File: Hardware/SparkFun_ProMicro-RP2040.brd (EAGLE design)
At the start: 17.8 x 33 mm, 109 parts, among them J2 Qwiic, J5 USB Female Type C Connector, U1 3.3V, U2 RP2040, U3 WS2812-2020, U4 W25QXX128MBIT, Y1 12MHz

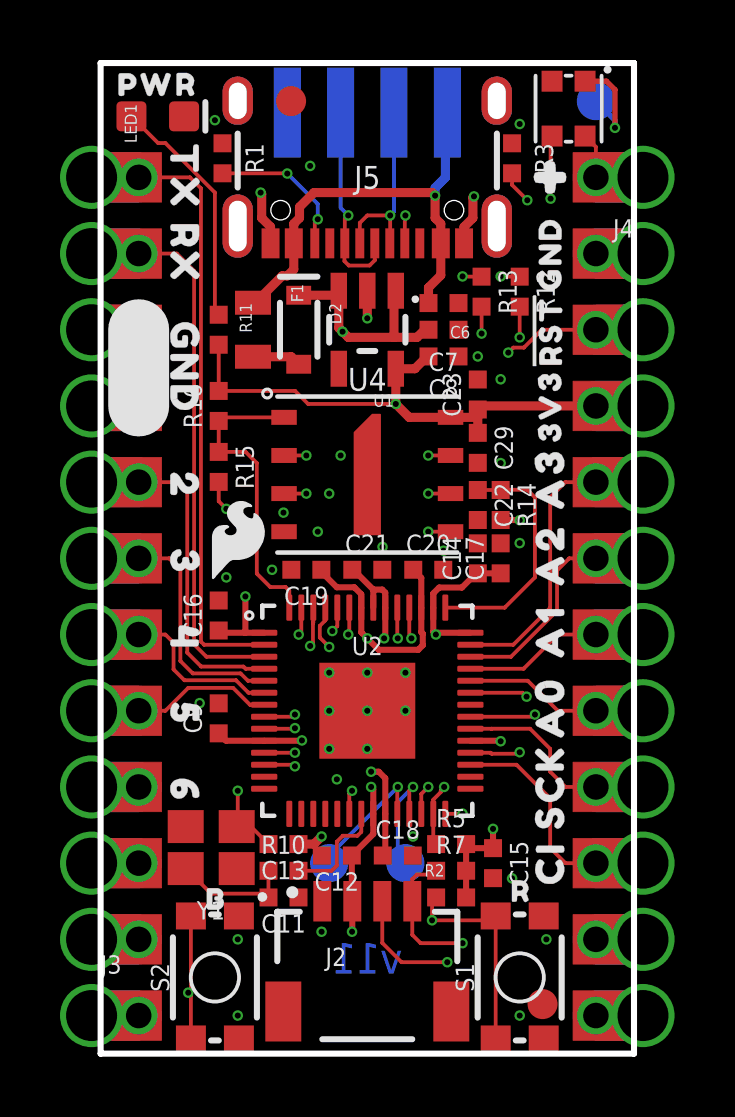
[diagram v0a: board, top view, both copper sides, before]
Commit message: Move passives for better DFM
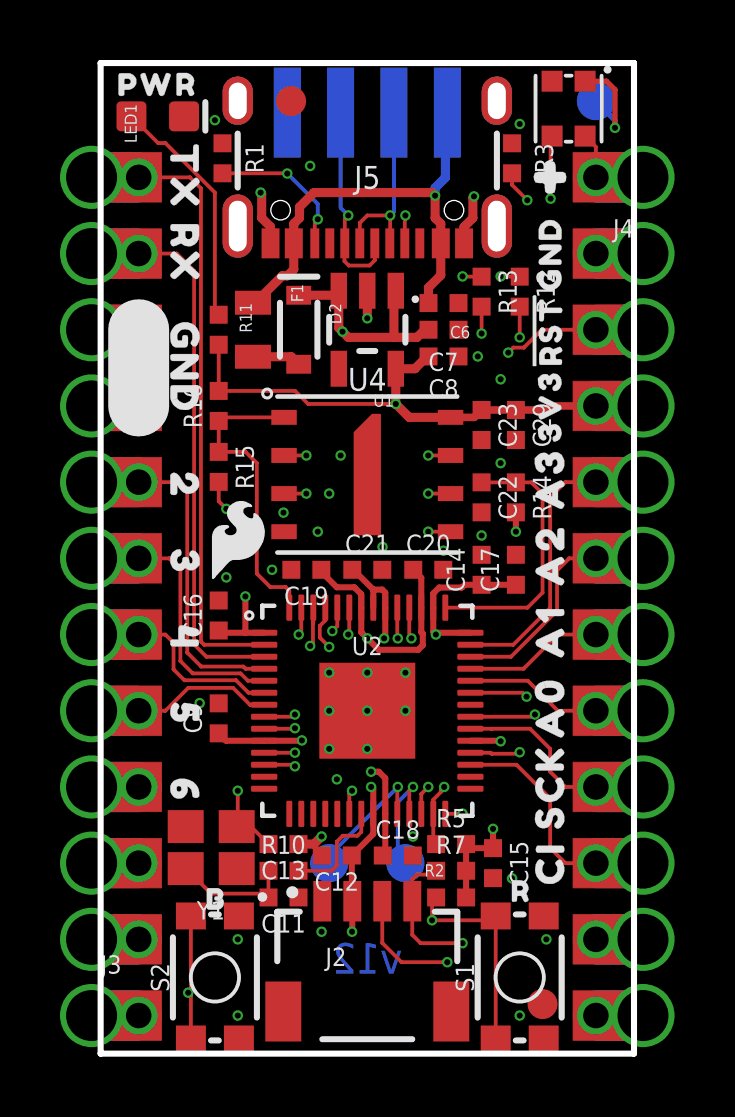
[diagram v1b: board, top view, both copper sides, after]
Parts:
- moved C29 1.48 mm to (13.8, 21.0)
- moved C23 1.02 mm to (12.7, 21.0), turned to 270 degrees
- moved C17 0.63 mm to (13.8, 16.1)
- moved R14 0.57 mm to (13.8, 18.5)
- moved C14 0.40 mm to (12.7, 16.1)
- moved C22 0.28 mm to (12.7, 18.5)
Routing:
- net ADC_VDD: track 8.09 -> 8.94 mm
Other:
- board text added: "v12"
- board text removed: "v11"

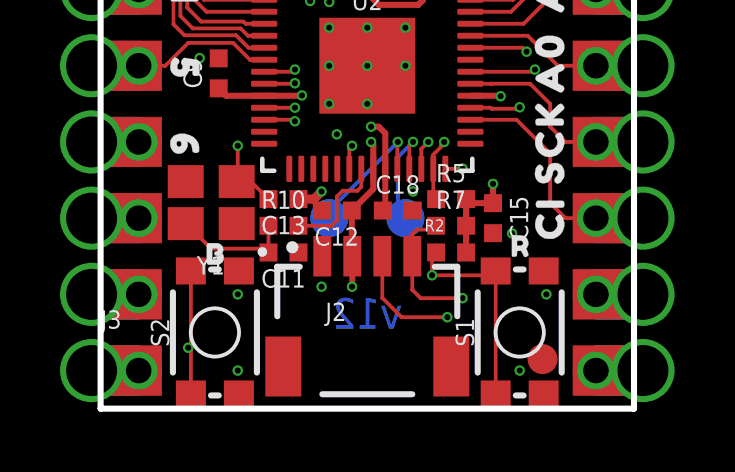
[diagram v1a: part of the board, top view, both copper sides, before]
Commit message: Increase isolation in layers 2/15. Increase to v13.
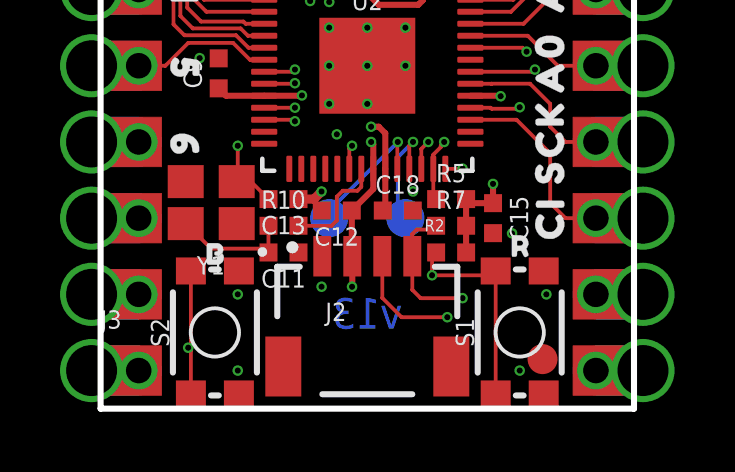
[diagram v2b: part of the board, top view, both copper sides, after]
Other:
- board text added: "Board Thickness is 0.8mm ENIG Finish"
- board text added: "v13"
- board text removed: "0.8mm PCB"
- board text removed: "v12"
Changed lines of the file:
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@@
 <setting verticaltext="up"/>
 </settings>
-<grid distance="1" unitdist="mm" unit="mm" style="lines" multiple="1" display="yes" altdistance="0.1" altunitdist="mm" altunit="mm"/>
+<grid distance="0.05" unitdist="inch" unit="inch" style="lines" multiple="1" display="yes" altdistance="0.005" altunitdist="inch" altunit="inch"/>
 <layers>
 <layer number="1" name="Top" color="4" fill="1" visible="yes" active="yes"/>
@@
 <layer number="47" name="Measures" color="7" fill="1" visible="no" active="yes"/>
 <layer number="48" name="Document" color="7" fill="1" visible="no" active="yes"/>
-<layer number="49" name="Reference" color="13" fill="1" visible="yes" active="yes"/>
+<layer number="49" name="Reference" color="13" fill="1" visible="no" active="yes"/>
 <layer number="50" name="dxf" color="7" fill="1" visible="no" active="yes"/>
 <layer number="51" name="tDocu" color="6" fill="1" visible="yes" active="yes"/>
@@
 <wire x1="17.78" y1="0" x2="17.78" y2="33.02" width="0.2032" layer="20"/>
 <wire x1="17.78" y1="33.02" x2="0" y2="33.02" width="0.2032" layer="20"/>
-<text x="8.89" y="3.175" size="1.016" layer="16" font="vector" ratio="25" rot="MR0" align="center">v12</text>
+<text x="8.89" y="3.175" size="1.016" layer="16" font="vector" ratio="25" rot="MR0" align="center">v13</text>
 <wire x1="1.27" y1="24.13" x2="1.27" y2="21.59" width="2.032" layer="21"/>
 <wire x1="1.27" y1="24.13" x2="1.27" y2="21.59" width="2.032" layer="22"/>
 <text x="73.66" y="-15.24" size="1.778" layer="51" font="vector" ratio="15">N Seidle</text>
-<text x="26.67" y="36.83" size="2.54" layer="51" font="vector" ratio="15">0.8mm PCB</text>
+<text x="25.4" y="35.56" size="1.778" layer="51" font="vector" ratio="15">Board Thickness is 0.8mm
+ENIG Finish</text>
 <dimension x1="0.02" y1="0" x2="0.02" y2="33.02" x3="-3.79" y3="16.51" textsize="1.778" textratio="15" layer="47" unit="inch"/>
 <dimension x1="1.29" y1="29.21" x2="0.02" y2="29.21" x3="0.655" y3="36.83" textsize="1.778" textratio="15" layer="47" unit="inch"/>
@@
 <text x="-2.52" y="-13.97" size="1.778" layer="47" font="vector" ratio="15">Units in Inches</text>
 <dimension x1="0.02" y1="33.02" x2="0.02" y2="34.29" x3="13.228" y3="33.655" textsize="1.778" textratio="15" layer="47" unit="inch"/>
-<wire x1="14.986" y1="-1.27" x2="14.986" y2="33.655" width="0.0254" layer="51"/>
-<wire x1="2.794" y1="-0.508" x2="2.794" y2="34.417" width="0.0254" layer="51"/>
 </plain>
 <attributes>
@@
 <wire x1="8.89" y1="25.4301" x2="8.89" y2="24.511" width="0.3048" layer="1"/>
 <via x="8.89" y="24.511" extent="1-16" drill="0.2"/>
-<polygon width="0.1016" layer="2" isolate="0.127">
+<polygon width="0.1016" layer="2" isolate="0.2032">
 <vertex x="0" y="33.02"/>
 <vertex x="17.78" y="33.02"/>
@@
 <wire x1="11.09" y1="14.056" x2="11.176" y2="13.97" width="0.2032" layer="1"/>
 <wire x1="18.08" y1="21.59" x2="16.51" y2="21.59" width="0.127" layer="1"/>
-<polygon width="0.1016" layer="15" isolate="0.127">
+<polygon width="0.1016" layer="15" isolate="0.2032">
 <vertex x="0" y="33.02"/>
 <vertex x="17.78" y="33.02"/>
@@
 </board>
 </drawing>
+<compatibility>
+<note version="6.3" minversion="6.2.2" severity="warning">
+Since Version 6.2.2 text objects can contain more than one line,
+which will not be processed correctly with this version.
+</note>
+</compatibility>
 </eagle>
